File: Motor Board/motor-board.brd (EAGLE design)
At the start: 60 x 26 mm, 13 parts

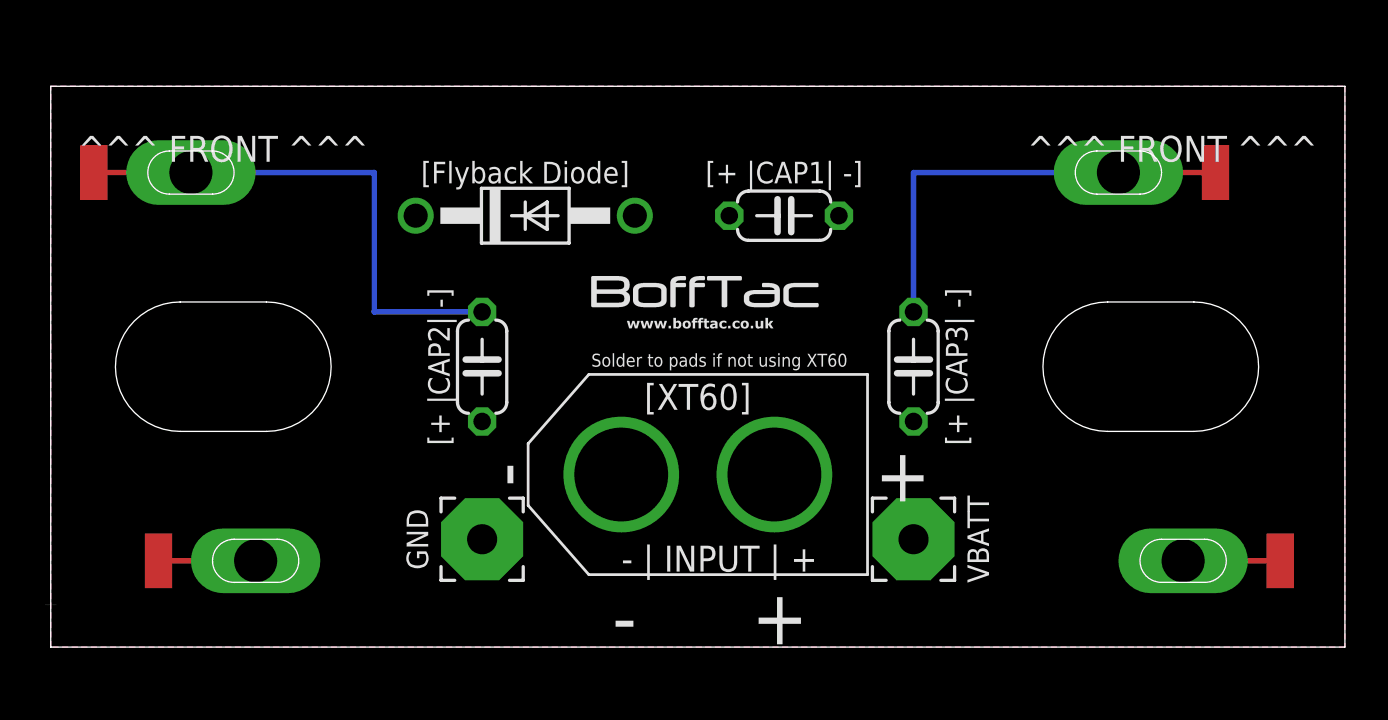
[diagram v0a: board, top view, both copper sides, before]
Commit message: Motor Board Update
16mm Gap and some other changes
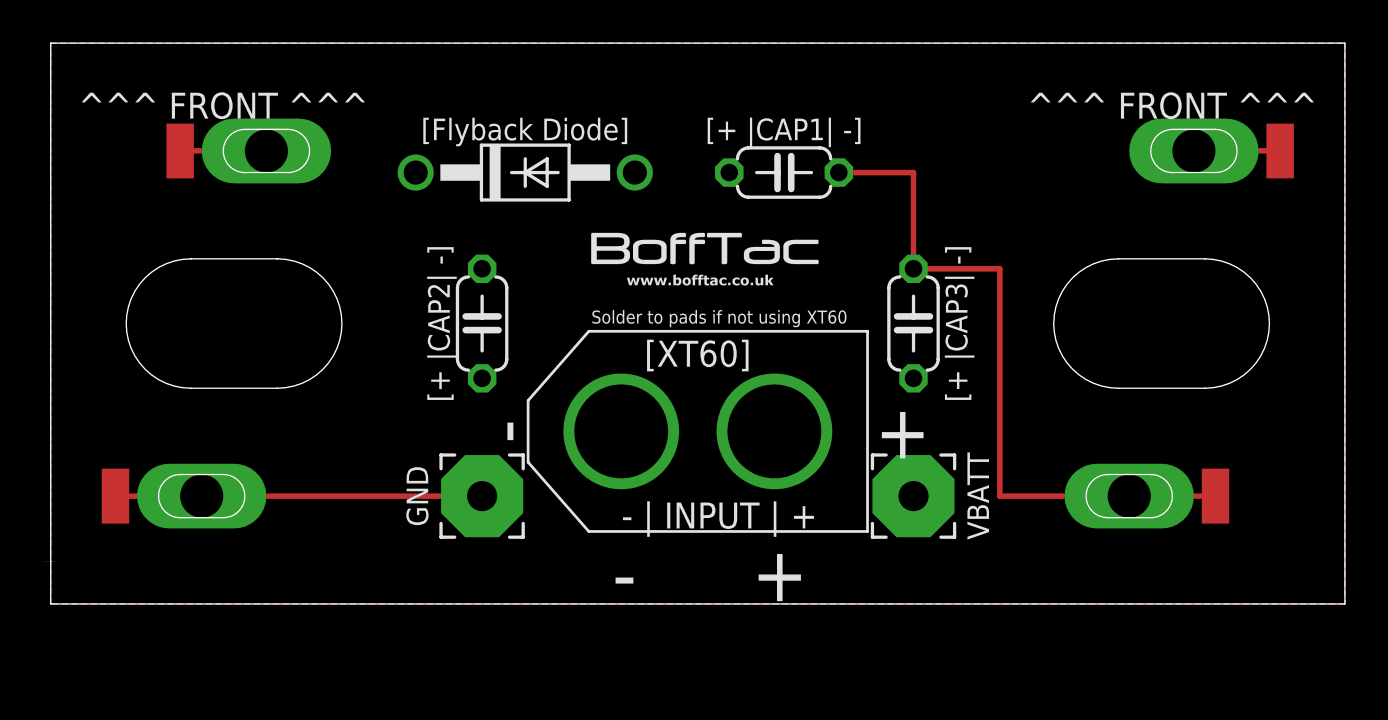
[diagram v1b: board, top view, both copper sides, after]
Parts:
- moved TOP-CAN 19.0 mm to (6.00, 21.0)
- moved BOTTOM-CAN 19.0 mm to (57.0, 21.0)
- moved PAD1 15.0 mm to (3.00, 5.00)
- moved PAD4 15.0 mm to (54.0, 5.00)
- moved U$1 2.50 mm to (9.00, 13.0), flipped to the top
- moved U$2 2.50 mm to (52.0, 13.0), flipped to the top
- moved C1 2.00 mm to (34.0, 20.0)
- moved C2 2.00 mm to (40.0, 13.0)
- moved C3 2.00 mm to (20.0, 13.0)
- moved D1 2.00 mm to (22.0, 20.0)
- moved J1 2.00 mm to (30.0, 8.00)
- moved PAD-GND 2.00 mm to (20.0, 5.00)
- moved PAD-VBATT 2.00 mm to (40.0, 5.00)
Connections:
- net GND: now also U$1.MOTOR+VE, U$2.MOTOR+VE; no longer U$1.MOTOR-VE, U$2.MOTOR-VE
- net VBATT: now also U$1.MOTOR-VE, U$2.MOTOR-VE; no longer U$1.MOTOR+VE, U$2.MOTOR+VE
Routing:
- net GND: track 44.9 -> 50.0 mm
- net VBATT: track 9.00 -> 8.00 mm
